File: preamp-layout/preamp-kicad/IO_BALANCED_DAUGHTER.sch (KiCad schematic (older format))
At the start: 49 parts, among them J24 XLR3, J25 XLR3, J26 Conn_01x03_Male, J27 Conn_01x03_Female, J28 Conn_01x03_Female, J29 Conn_01x03_Male, J30 XLR3, J31 XLR3, U6 TL072, U7 TL072, U8 TL072

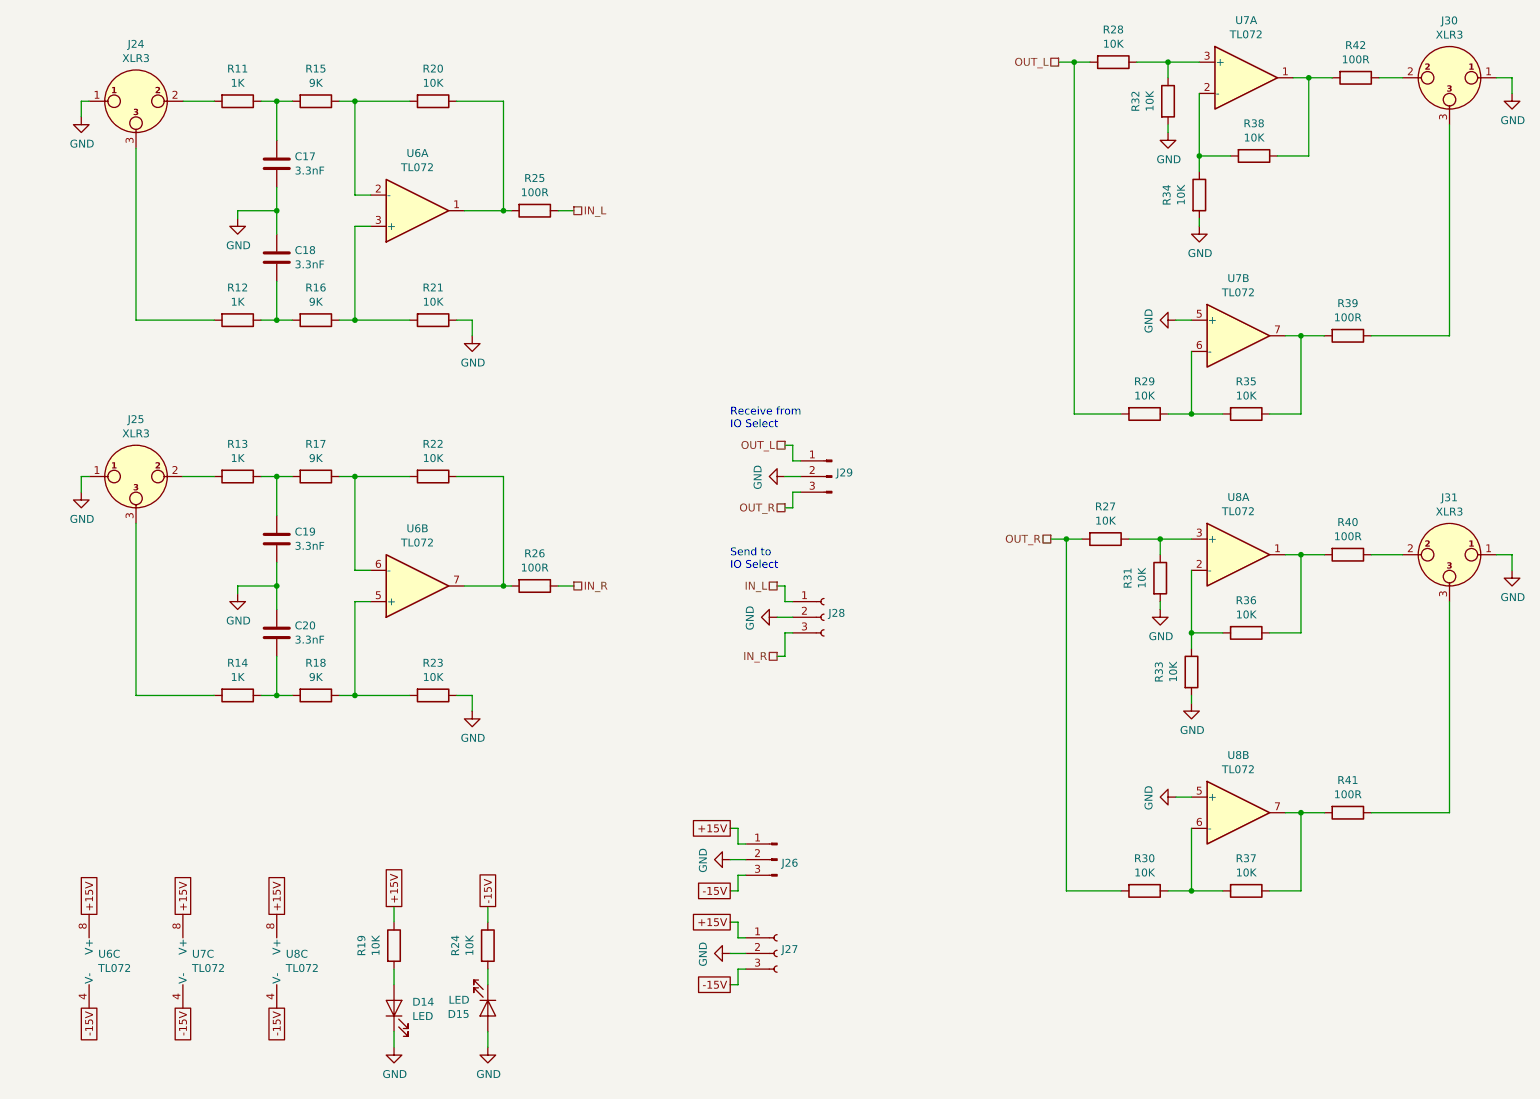
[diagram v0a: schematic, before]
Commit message: AC PCB Update
Removed Switch symbol from PCB, moved to main sheet. Started playing with footprint assignment. Other minor updates.
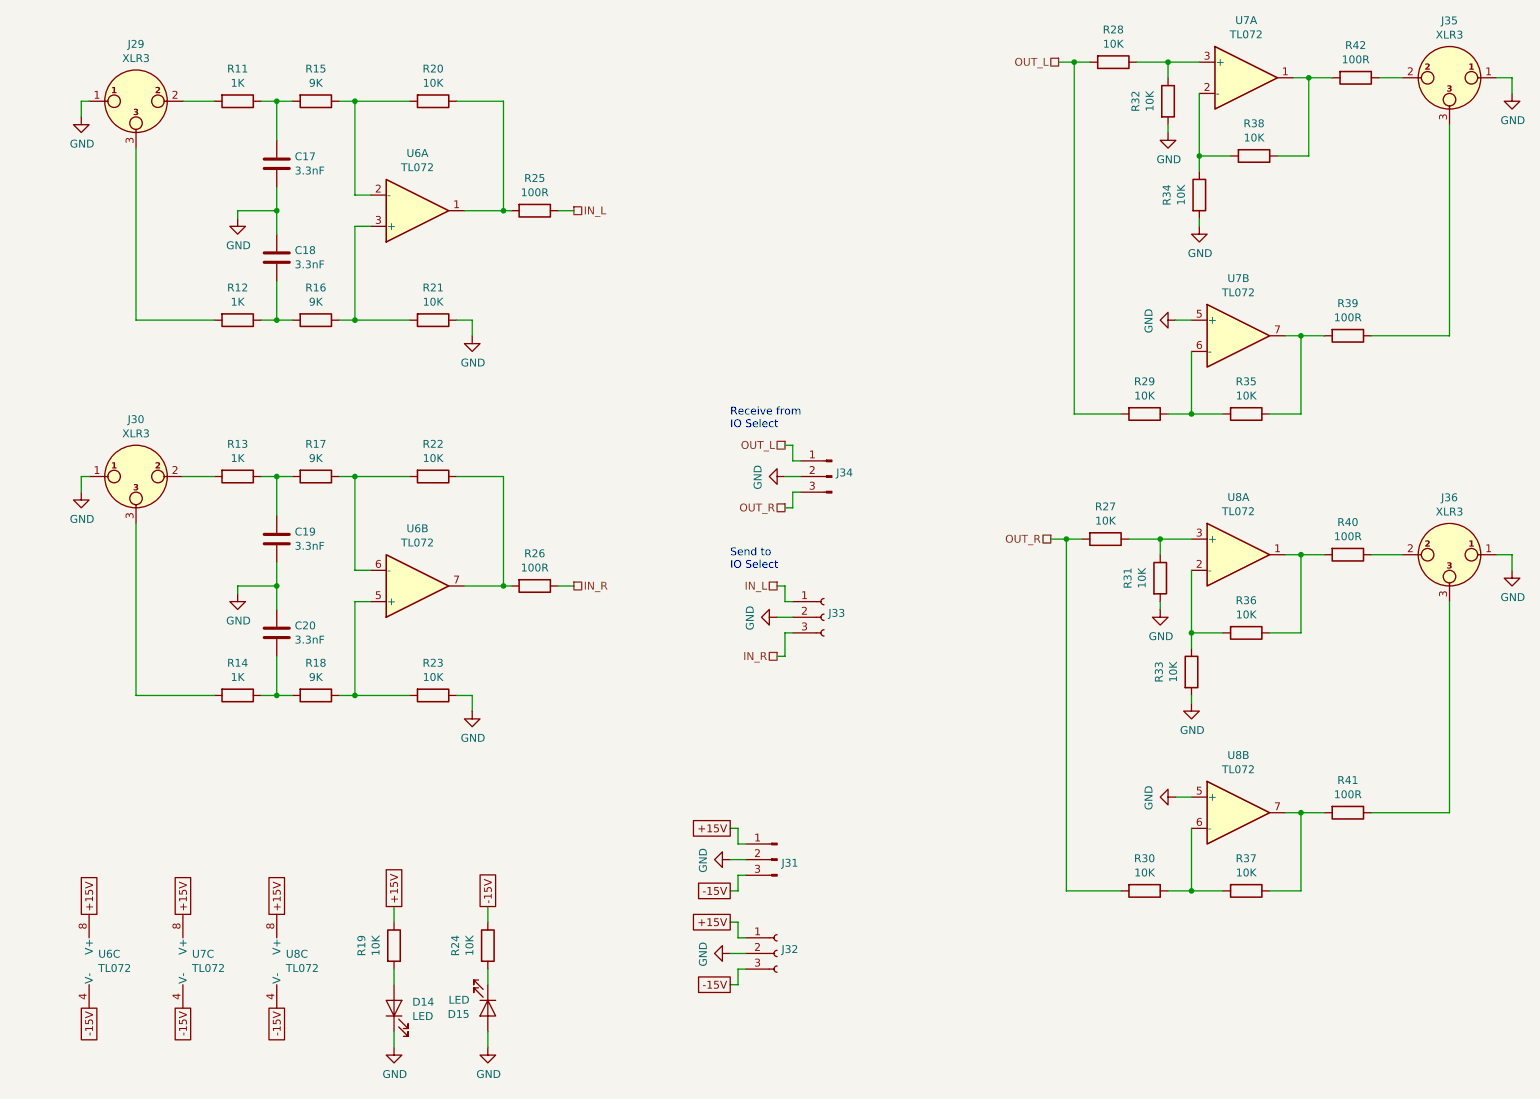
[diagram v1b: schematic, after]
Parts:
- renumbered J24 to J29, J25 to J30, J26 to J31, J27 to J32, J28 to J33, J29 to J34, J30 to J35, J31 to J36
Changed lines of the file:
@@
 AR Path="/5E2D8DA2/5E226783" Ref="J?"  Part="1"
 AR Path="/5E607732/5E226783" Ref="J?"  Part="1"
-AR Path="/5E1A0CE1/5E226783" Ref="J24"  Part="1"
+AR Path="/5E1A0CE1/5E226783" Ref="J29"  Part="1"
 AR Path="/5E80BFEC/5E226783" Ref="J?"  Part="1"
-F 0 "J24" H 1800 1615 50  0000 C CNN
+F 0 "J29" H 1800 1615 50  0000 C CNN
 F 1 "XLR3" H 1800 1524 50  0000 C CNN
 F 2 "" H 1800 1250 50  0001 C CNN
@@
 AR Path="/5E2D8DA2/5E2267AB" Ref="J?"  Part="1"
 AR Path="/5E607732/5E2267AB" Ref="J?"  Part="1"
-AR Path="/5E1A0CE1/5E2267AB" Ref="J25"  Part="1"
+AR Path="/5E1A0CE1/5E2267AB" Ref="J30"  Part="1"
 AR Path="/5E80BFEC/5E2267AB" Ref="J?"  Part="1"
-F 0 "J25" H 1800 4015 50  0000 C CNN
+F 0 "J30" H 1800 4015 50  0000 C CNN
 F 1 "XLR3" H 1800 3924 50  0000 C CNN
 F 2 "" H 1800 3650 50  0001 C CNN
@@
 AR Path="/5E2D8DA2/5E2267D3" Ref="J?"  Part="1"
 AR Path="/5E607732/5E2267D3" Ref="J?"  Part="1"
-AR Path="/5E1A0CE1/5E2267D3" Ref="J30"  Part="1"
+AR Path="/5E1A0CE1/5E2267D3" Ref="J35"  Part="1"
 AR Path="/5E80BFEC/5E2267D3" Ref="J?"  Part="1"
-F 0 "J30" H 10200 1465 50  0000 C CNN
+F 0 "J35" H 10200 1465 50  0000 C CNN
 F 1 "XLR3" H 10200 1374 50  0000 C CNN
 F 2 "" H 10200 1100 50  0001 C CNN
@@
 AR Path="/5E2D8DA2/5E40412B" Ref="J?"  Part="1"
 AR Path="/5E607732/5E40412B" Ref="J?"  Part="1"
-AR Path="/5E1A0CE1/5E40412B" Ref="J31"  Part="1"
+AR Path="/5E1A0CE1/5E40412B" Ref="J36"  Part="1"
 AR Path="/5E80BFEC/5E40412B" Ref="J?"  Part="1"
-F 0 "J31" H 10200 4515 50  0000 C CNN
+F 0 "J36" H 10200 4515 50  0000 C CNN
 F 1 "XLR3" H 10200 4424 50  0000 C CNN
 F 2 "" H 10200 4150 50  0001 C CNN
@@
 AR Path="/5E607732/643B9E8C" Ref="J?"  Part="1"
 AR Path="/5E2D8DA2/643B9E8C" Ref="J?"  Part="1"
-AR Path="/5E1A0CE1/643B9E8C" Ref="J28"  Part="1"
-F 0 "J28" H 6228 4576 50  0000 L CNN
+AR Path="/5E1A0CE1/643B9E8C" Ref="J33"  Part="1"
+F 0 "J33" H 6228 4576 50  0000 L CNN
 F 1 "Conn_01x03_Female" H 6228 4485 50  0001 L CNN
 F 2 "" H 6200 4550 50  0001 C CNN
@@
 P 6250 3650
 AR Path="/5E2D8DA2/643B9E92" Ref="J?"  Part="1"
-AR Path="/5E1A0CE1/643B9E92" Ref="J29"  Part="1"
-F 0 "J29" H 6222 3674 50  0000 R CNN
+AR Path="/5E1A0CE1/643B9E92" Ref="J34"  Part="1"
+F 0 "J34" H 6222 3674 50  0000 R CNN
 F 1 "Conn_01x03_Male" H 6222 3583 50  0001 R CNN
 F 2 "" H 6250 3650 50  0001 C CNN
@@
 AR Path="/5E27B612/64789762" Ref="J?"  Part="1"
 AR Path="/6009D432/64789762" Ref="J?"  Part="1"
-AR Path="/5E1A0CE1/64789762" Ref="J26"  Part="1"
-F 0 "J26" H 5872 6078 50  0000 R CNN
+AR Path="/5E1A0CE1/64789762" Ref="J31"  Part="1"
+F 0 "J31" H 5872 6078 50  0000 R CNN
 F 1 "Conn_01x03_Male" H 5872 6033 50  0001 R CNN
 F 2 "" H 5900 6100 50  0001 C CNN
@@
 AR Path="/5E2D8DA2/64789768" Ref="J?"  Part="1"
 AR Path="/6009D432/64789768" Ref="J?"  Part="1"
-AR Path="/5E1A0CE1/64789768" Ref="J27"  Part="1"
-F 0 "J27" H 5928 6726 50  0000 L CNN
+AR Path="/5E1A0CE1/64789768" Ref="J32"  Part="1"
+F 0 "J32" H 5928 6726 50  0000 L CNN
 F 1 "Conn_01x03_Female" H 5928 6635 50  0001 L CNN
 F 2 "" H 5900 6700 50  0001 C CNN

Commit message: Initial Footprint Assignment
Assigned footprints to SMT resistors, pin headers, screw terminals, LEDs, DIP-8 ICs
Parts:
- D14, D15: footprint (none) -> LED_SMD:LED_1206_3216Metric_Pad1.42x1.75mm_HandSolder
- J31, J32, J33, J34: footprint (none) -> Connector_PinHeader_2.54mm:PinHeader_1x03_P2.54mm_Vertical
- R11, R12, R13, R14, R15, R16, R17, R18, R19, R20, R21, R22, R23, R24, R25, R26, R27, R28, R29, R30, R31, R32, R33, R34, R35, R36, R37, R38, R39, R40, R41, R42: footprint (none) -> Resistor_SMD:R_1206_3216Metric_Pad1.42x1.75mm_HandSolder
- U6, U7, U8: footprint (none) -> Package_DIP:DIP-8_W7.62mm_Socket_LongPads

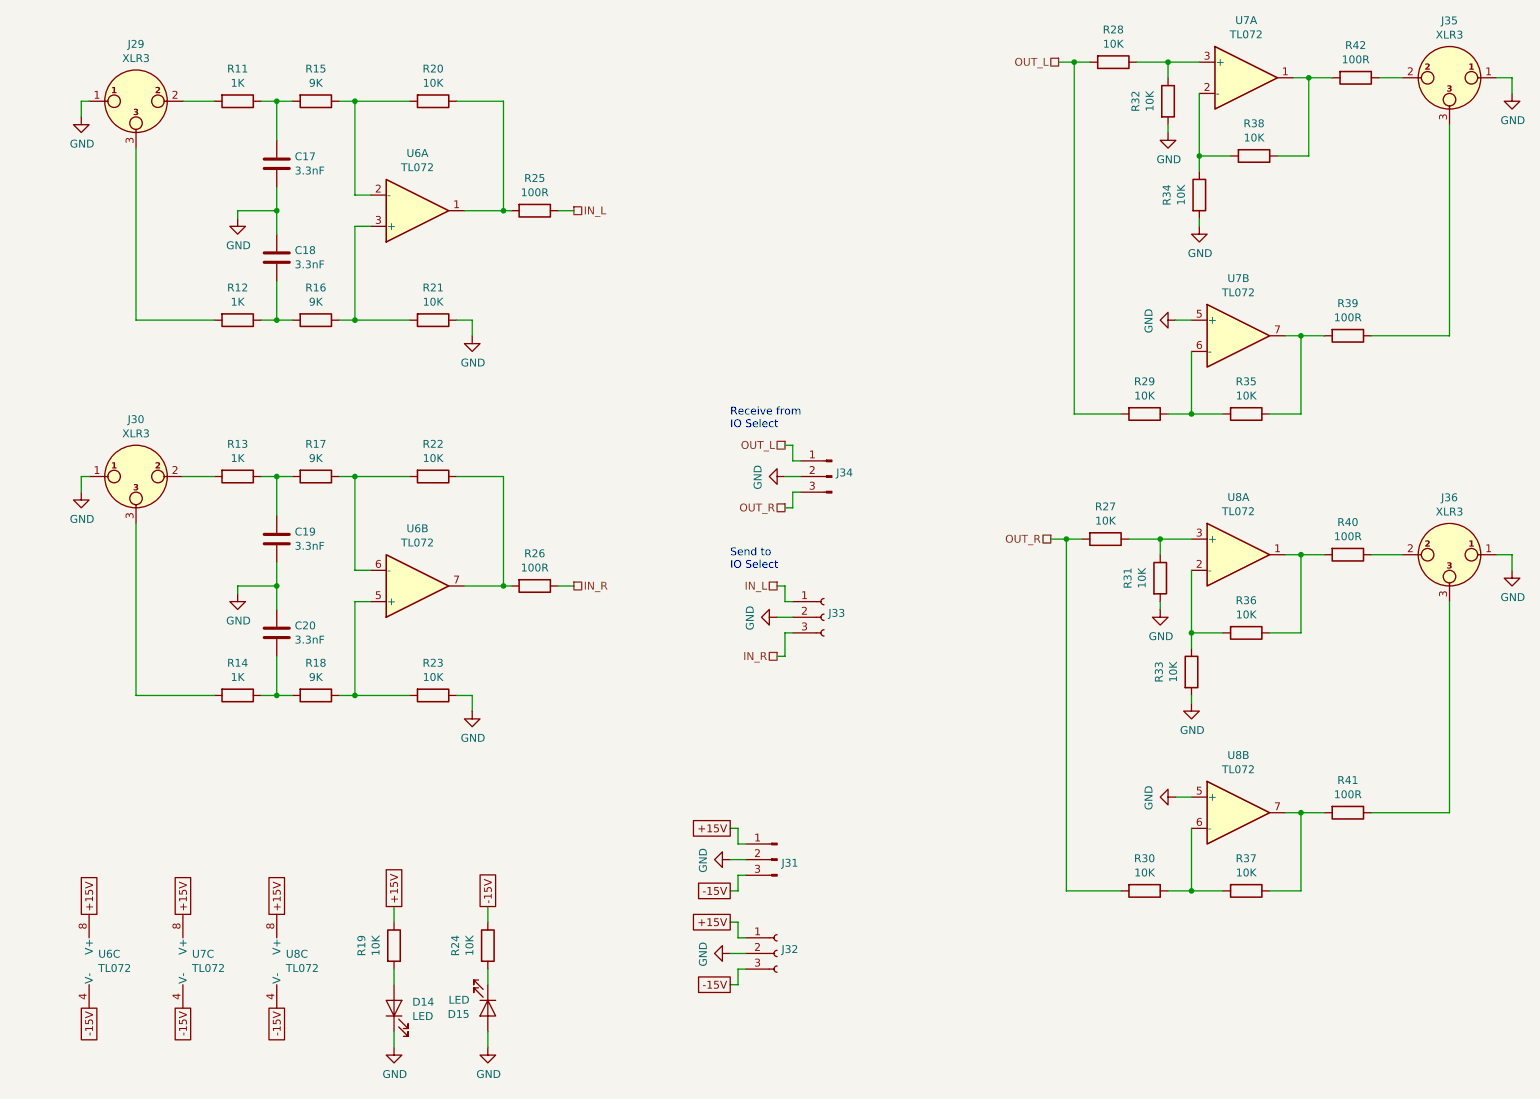
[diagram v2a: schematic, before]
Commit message: BOM update
Minor changes to schematic, value changes and footprint entry. BOM updated with parts sourcing
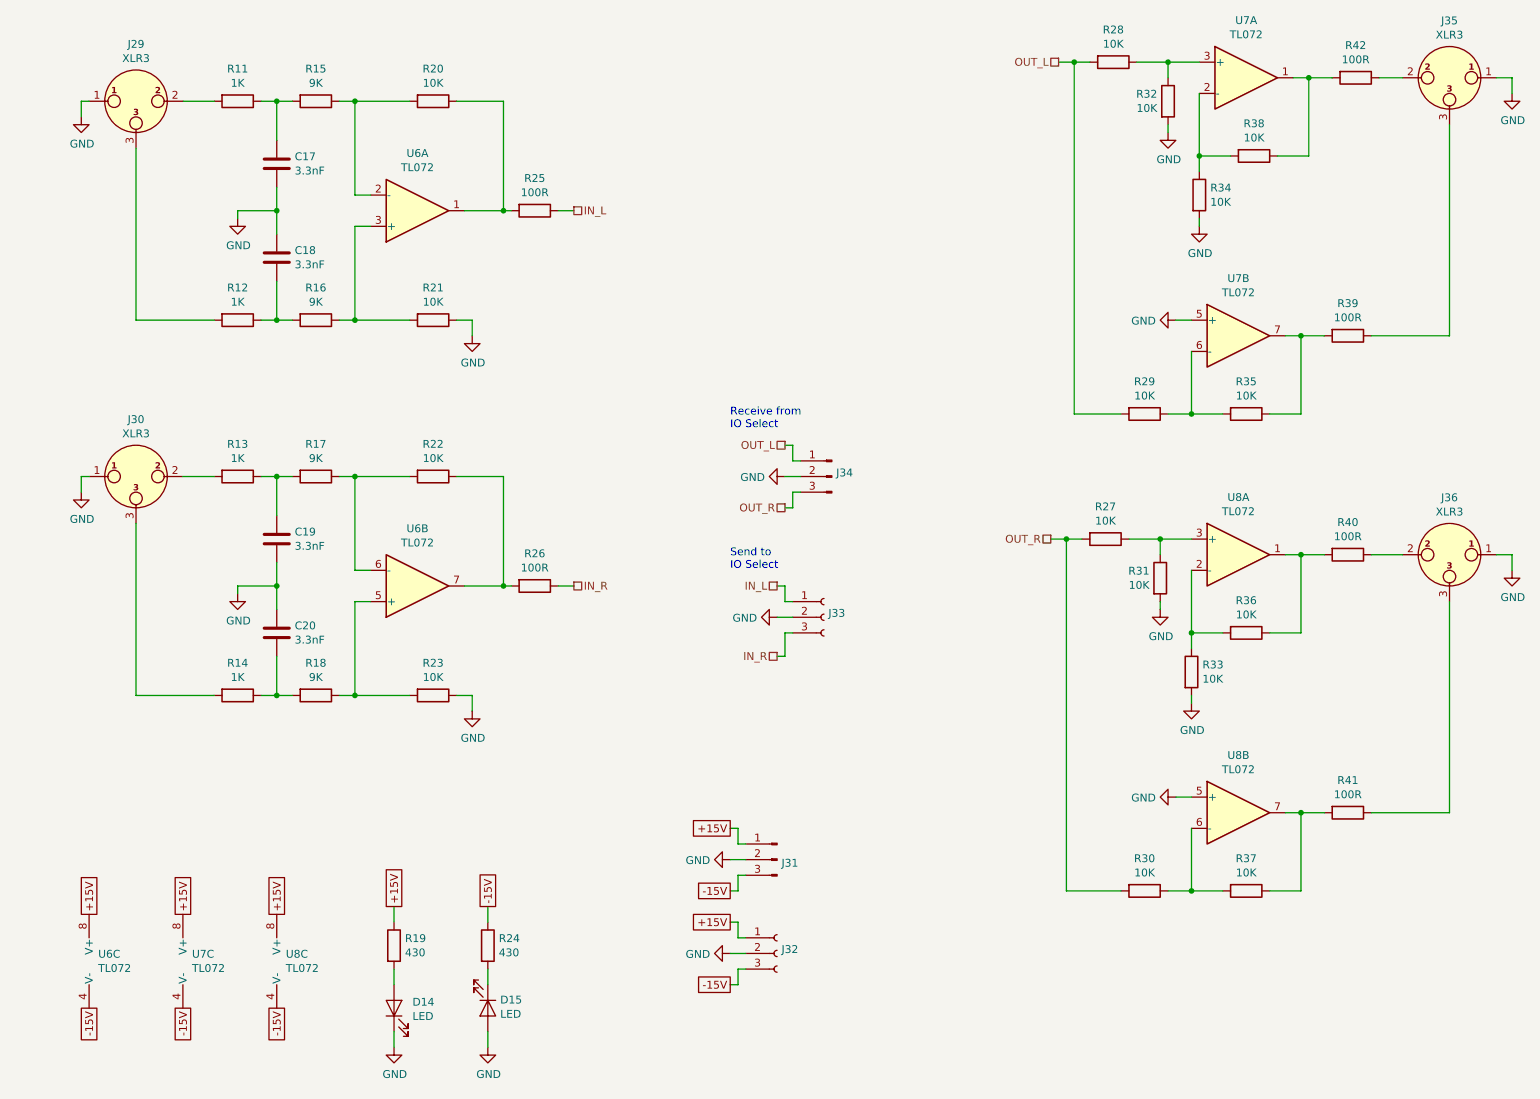
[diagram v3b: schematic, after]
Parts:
- R19, R24: value 10K -> 430
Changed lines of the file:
@@
 AR Path="/5E1A0CE1/5E1BDEF1" Ref="R32"  Part="1"
 AR Path="/5E80BFEC/5E1BDEF1" Ref="R?"  Part="1"
-F 0 "R32" V 8193 1250 50  0000 C CNN
-F 1 "10K" V 8284 1250 50  0000 C CNN
+F 0 "R32" H 8331 1296 50  0000 R CNN
+F 1 "10K" H 8331 1205 50  0000 R CNN
 F 2 "Resistor_SMD:R_1206_3216Metric_Pad1.42x1.75mm_HandSolder" V 8330 1250 50  0001 C CNN
 F 3 "~" H 8400 1250 50  0001 C CNN
@@
 AR Path="/5E1A0CE1/5E1BDF16" Ref="R34"  Part="1"
 AR Path="/5E80BFEC/5E1BDF16" Ref="R?"  Part="1"
-F 0 "R34" V 8393 1850 50  0000 C CNN
-F 1 "10K" V 8484 1850 50  0000 C CNN
+F 0 "R34" H 8670 1896 50  0000 L CNN
+F 1 "10K" H 8670 1805 50  0000 L CNN
 F 2 "Resistor_SMD:R_1206_3216Metric_Pad1.42x1.75mm_HandSolder" V 8530 1850 50  0001 C CNN
 F 3 "~" H 8600 1850 50  0001 C CNN
@@
 AR Path="/5E1A0CE1/5E1BDF33" Ref="R31"  Part="1"
 AR Path="/5E80BFEC/5E1BDF33" Ref="R?"  Part="1"
-F 0 "R31" V 8143 4300 50  0000 C CNN
-F 1 "10K" V 8234 4300 50  0000 C CNN
+F 0 "R31" H 8281 4346 50  0000 R CNN
+F 1 "10K" H 8281 4255 50  0000 R CNN
 F 2 "Resistor_SMD:R_1206_3216Metric_Pad1.42x1.75mm_HandSolder" V 8280 4300 50  0001 C CNN
 F 3 "~" H 8350 4300 50  0001 C CNN
@@
 AR Path="/5E1A0CE1/5E1BDF58" Ref="R33"  Part="1"
 AR Path="/5E80BFEC/5E1BDF58" Ref="R?"  Part="1"
-F 0 "R33" V 8343 4900 50  0000 C CNN
-F 1 "10K" V 8434 4900 50  0000 C CNN
+F 0 "R33" H 8620 4946 50  0000 L CNN
+F 1 "10K" H 8620 4855 50  0000 L CNN
 F 2 "Resistor_SMD:R_1206_3216Metric_Pad1.42x1.75mm_HandSolder" V 8480 4900 50  0001 C CNN
 F 3 "~" H 8550 4900 50  0001 C CNN
@@
 AR Path="/5E1A0CE1/5E50A27F" Ref="R19"  Part="1"
 AR Path="/5E80BFEC/5E50A27F" Ref="R?"  Part="1"
-F 0 "R19" V 3243 6650 50  0000 C CNN
-F 1 "10K" V 3334 6650 50  0000 C CNN
+F 0 "R19" H 3520 6696 50  0000 L CNN
+F 1 "430" H 3520 6605 50  0000 L CNN
 F 2 "Resistor_SMD:R_1206_3216Metric_Pad1.42x1.75mm_HandSolder" V 3380 6650 50  0001 C CNN
 F 3 "~" H 3450 6650 50  0001 C CNN
@@
 AR Path="/5E1A0CE1/5E50A285" Ref="D14"  Part="1"
 AR Path="/5E80BFEC/5E50A285" Ref="D?"  Part="1"
-F 0 "D14" V 3489 6933 50  0000 R CNN
-F 1 "LED" V 3398 6933 50  0000 R CNN
+F 0 "D14" V 3489 6932 50  0000 R CNN
+F 1 "LED" V 3398 6932 50  0000 R CNN
 F 2 "LED_SMD:LED_1206_3216Metric_Pad1.42x1.75mm_HandSolder" H 3450 7050 50  0001 C CNN
 F 3 "~" H 3450 7050 50  0001 C CNN
@@
 AR Path="/5E1A0CE1/5E50A28F" Ref="R24"  Part="1"
 AR Path="/5E80BFEC/5E50A28F" Ref="R?"  Part="1"
-F 0 "R24" V 3843 6650 50  0000 C CNN
-F 1 "10K" V 3934 6650 50  0000 C CNN
+F 0 "R24" H 4120 6696 50  0000 L CNN
+F 1 "430" H 4120 6605 50  0000 L CNN
 F 2 "Resistor_SMD:R_1206_3216Metric_Pad1.42x1.75mm_HandSolder" V 3980 6650 50  0001 C CNN
 F 3 "~" H 4050 6650 50  0001 C CNN
@@
 AR Path="/5E1A0CE1/5E50A295" Ref="D15"  Part="1"
 AR Path="/5E80BFEC/5E50A295" Ref="D?"  Part="1"
-F 0 "D15" V 4089 6933 50  0000 R CNN
-F 1 "LED" V 3998 6933 50  0000 R CNN
+F 0 "D15" V 3997 7129 50  0000 L CNN
+F 1 "LED" V 4088 7129 50  0000 L CNN
 F 2 "LED_SMD:LED_1206_3216Metric_Pad1.42x1.75mm_HandSolder" H 4050 7050 50  0001 C CNN
 F 3 "~" H 4050 7050 50  0001 C CNN
@@
 AR Path="/5E1A0CE1/64A55E9B" Ref="#PWR035"  Part="1"
 F 0 "#PWR035" H 5600 5850 50  0001 C CNN
-F 1 "GND" H 5605 5927 50  0000 C CNN
+F 1 "GND" V 5605 5972 50  0000 R CNN
 F 2 "" H 5600 6100 50  0001 C CNN
 F 3 "" H 5600 6100 50  0001 C CNN
@@
 AR Path="/5E1A0CE1/64A786FB" Ref="#PWR036"  Part="1"
 F 0 "#PWR036" H 5600 6450 50  0001 C CNN
-F 1 "GND" H 5605 6527 50  0000 C CNN
+F 1 "GND" V 5605 6572 50  0000 R CNN
 F 2 "" H 5600 6700 50  0001 C CNN
 F 3 "" H 5600 6700 50  0001 C CNN
@@
 AR Path="/5E1A0CE1/64A7FA93" Ref="#PWR037"  Part="1"
 F 0 "#PWR037" H 5900 4300 50  0001 C CNN
-F 1 "GND" H 5905 4377 50  0000 C CNN
+F 1 "GND" V 5905 4422 50  0000 R CNN
 F 2 "" H 5900 4550 50  0001 C CNN
 F 3 "" H 5900 4550 50  0001 C CNN
@@
 AR Path="/5E1A0CE1/64A9A3E0" Ref="#PWR038"  Part="1"
 F 0 "#PWR038" H 5950 3400 50  0001 C CNN
-F 1 "GND" H 5955 3477 50  0000 C CNN
+F 1 "GND" V 5955 3522 50  0000 R CNN
 F 2 "" H 5950 3650 50  0001 C CNN
 F 3 "" H 5950 3650 50  0001 C CNN
@@
 AR Path="/5E1A0CE1/64B44F34" Ref="#PWR041"  Part="1"
 F 0 "#PWR041" H 8450 2400 50  0001 C CNN
-F 1 "GND" H 8455 2477 50  0000 C CNN
+F 1 "GND" V 8455 2522 50  0000 R CNN
 F 2 "" H 8450 2650 50  0001 C CNN
 F 3 "" H 8450 2650 50  0001 C CNN
@@
 AR Path="/5E1A0CE1/64B7CB4A" Ref="#PWR042"  Part="1"
 F 0 "#PWR042" H 8450 5450 50  0001 C CNN
-F 1 "GND" H 8455 5527 50  0000 C CNN
+F 1 "GND" V 8455 5572 50  0000 R CNN
 F 2 "" H 8450 5700 50  0001 C CNN
 F 3 "" H 8450 5700 50  0001 C CNN
